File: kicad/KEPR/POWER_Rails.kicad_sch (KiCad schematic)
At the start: 21 parts, among them J1 PINHD_1x20_Male, J12 PINHD_1x20_Male, J13 PINHD_1x20_Male, J14 PINHD_1x20_Male, J15 PINHD_1x20_Male, J16 PINHD_1x10_Male, J17 PINHD_1x20_Male, J18 PINHD_1x20_Male, J19 PINHD_1x20_Male, J2 PINHD_1x20_Male, J20 PINHD_1x20_Male, J21 PINHD_1x20_Male, J22 PINHD_1x20_Male, J23 PINHD_1x10_Male, J24 PINHD_2x3_Male, J25 PINHD_2x3_Male, J26 PINHD_2x3_Male, J27 PINHD_2x3_Male, J28 PINHD_2x3_Male, J29 PINHD_2x3_Male, J30 PINHD_2x3_Male

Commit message: mais ajustes no power rail inclusive com imagem 3d
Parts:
- removed J14, J15, J21, J22: PINHD_1x20_Male, Connector_PinHeader_2.54mm:PinHeader_1x20_P2.54mm_Vertical, symbol PCM_SL_Pin_Headers:PINHD_1x20_Male
- removed J28, J29: PINHD_2x3_Male, Connector_PinHeader_2.54mm:PinHeader_2x03_P2.54mm_Vertical, symbol PCM_SL_Pin_Headers:PINHD_2x3_Male
- added J14: PINHD_2x3_Male, Connector_PinHeader_2.54mm:PinHeader_2x03_P2.54mm_Vertical, symbol PCM_SL_Pin_Headers:PINHD_2x3_Male
- added J15, J21: PINHD_1x10_Male, Connector_PinHeader_2.54mm:PinHeader_1x10_P2.54mm_Vertical, symbol PCM_SL_Pin_Headers:PINHD_1x10_Male
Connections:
- net +12V: now also J14.2
- net +3.3V: now also J14.6
- net +5V: now also J14.4
- net GND: now also J21.1, J21.10, J21.2, J21.3, J21.4, J21.5, J21.6, J21.7, J21.8, J21.9
- new net: J14.1, J14.3, J14.5, J15.1, J15.10, J15.2, J15.3, J15.4, J15.5, J15.6, J15.7, J15.8, J15.9
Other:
- moved on the sheet: J1, J12, J16, J17, J18, J19, J2, J20, J23, J24, J25, J26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

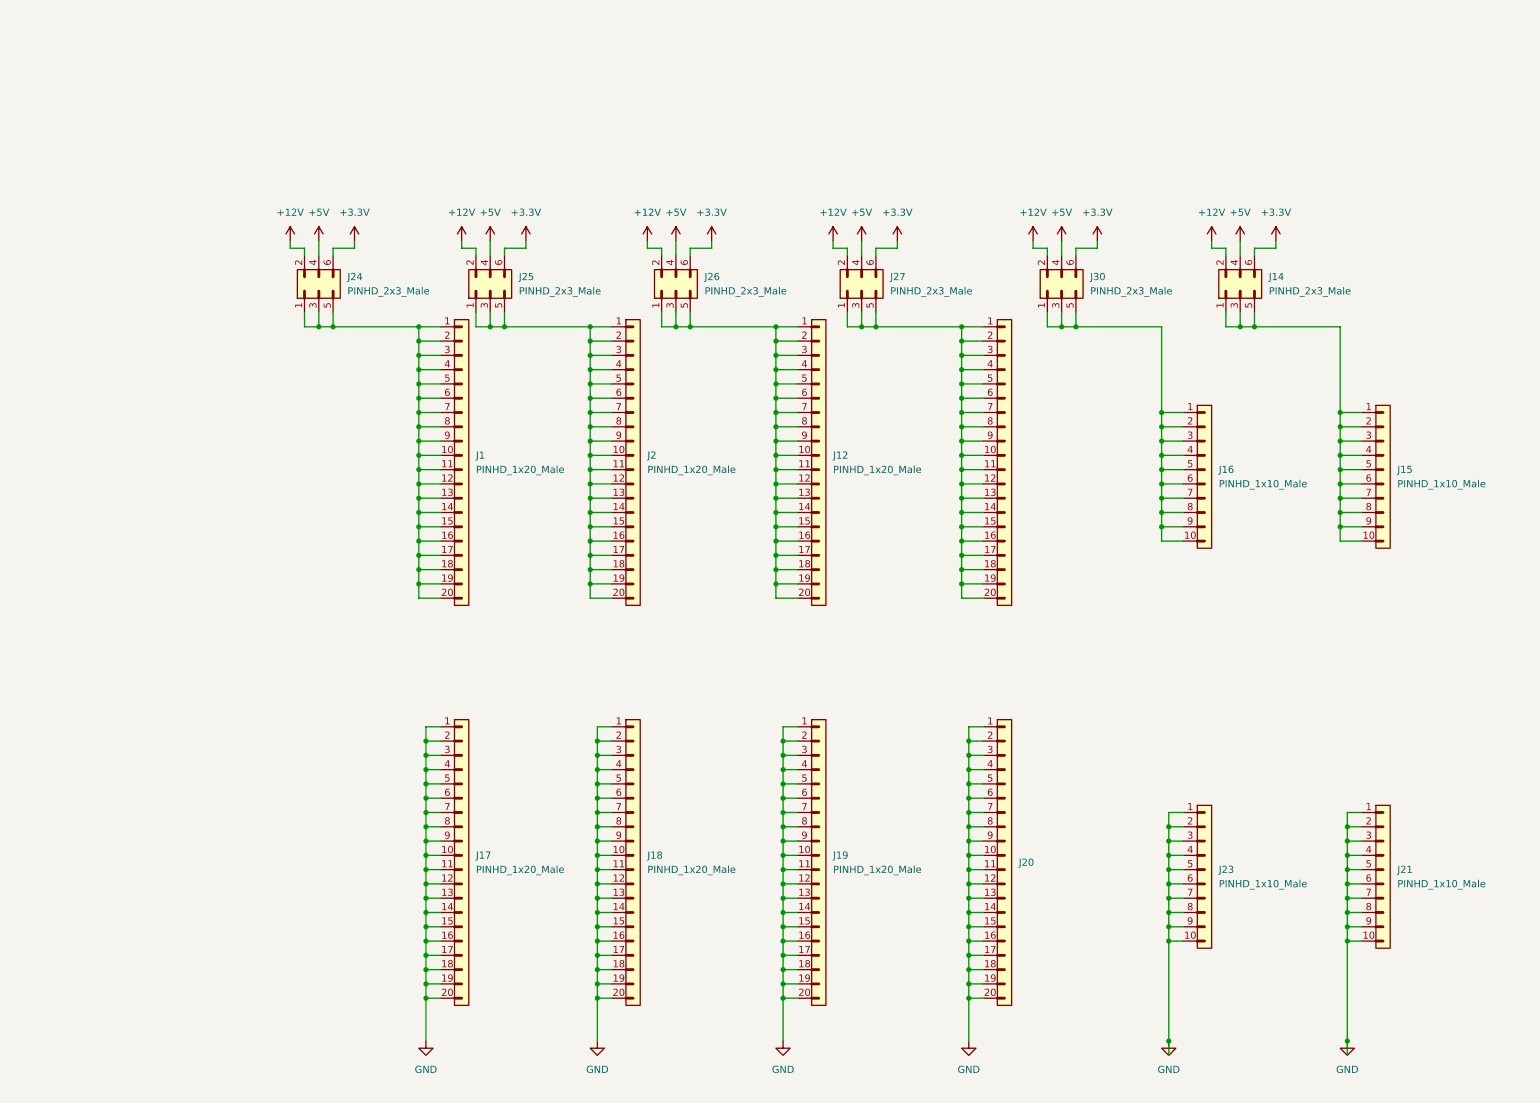
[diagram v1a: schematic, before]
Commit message: Mais ajustes nas folhas de esquemático no Power Rails
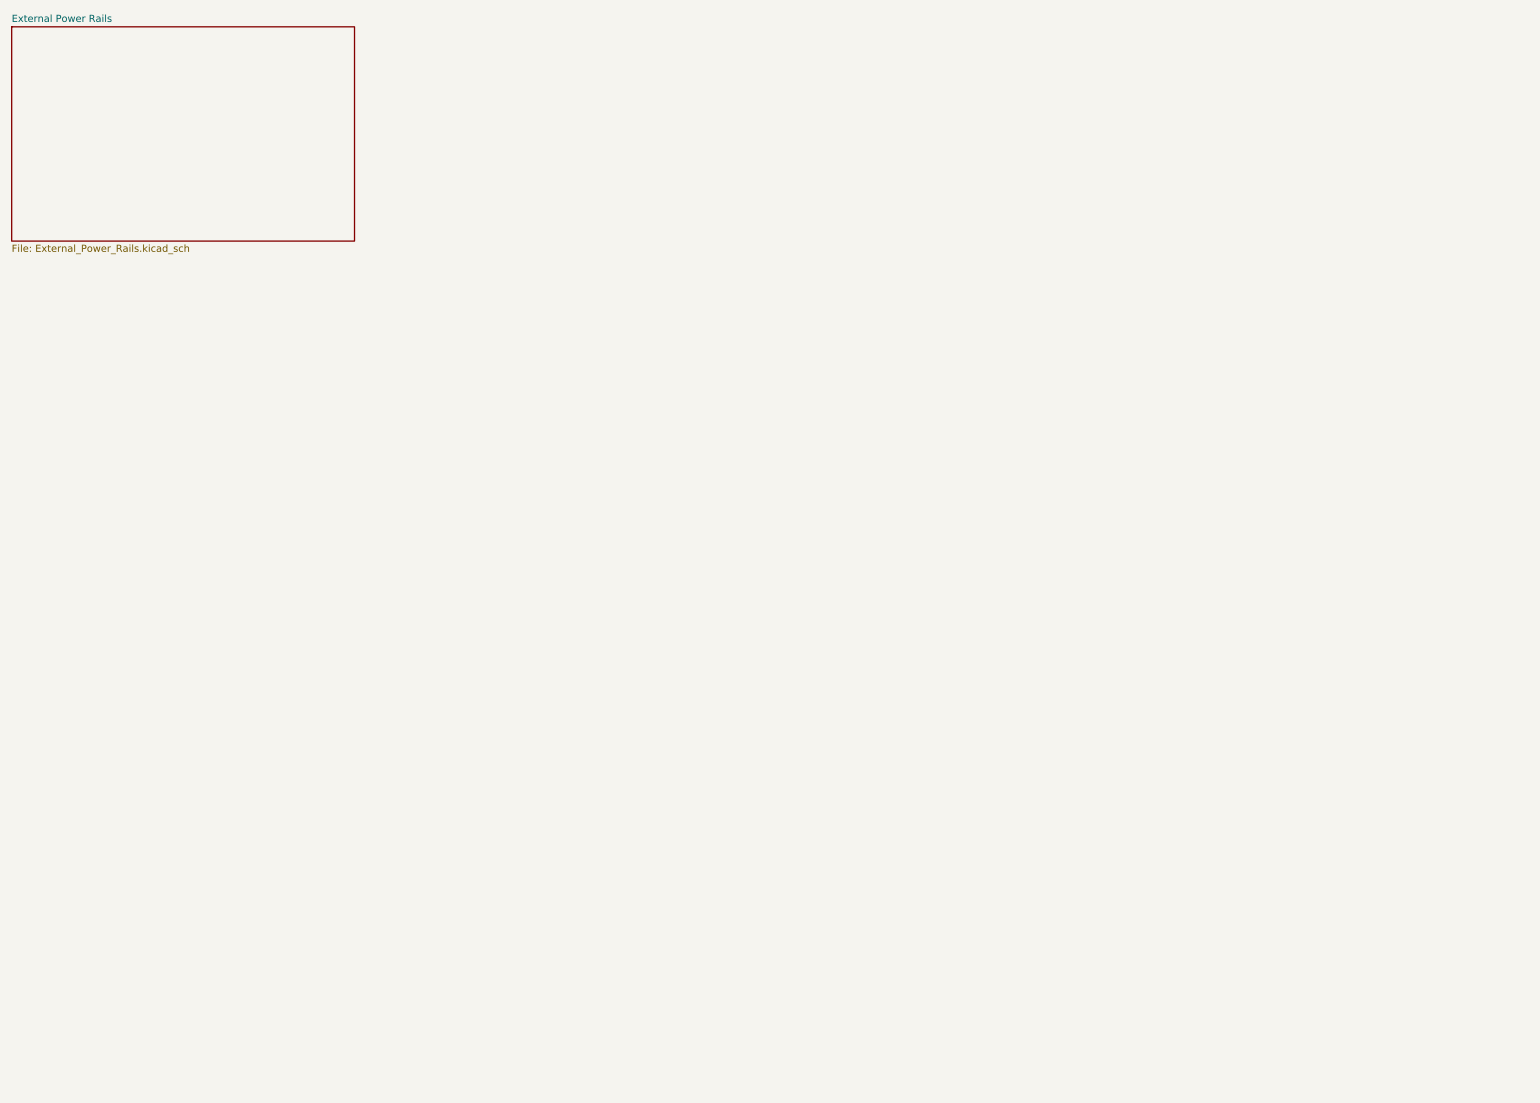
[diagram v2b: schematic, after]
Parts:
- removed J1, J12, J13, J17, J18, J19, J2, J20: PINHD_1x20_Male, Connector_PinHeader_2.54mm:PinHeader_1x20_P2.54mm_Vertical, symbol PCM_SL_Pin_Headers:PINHD_1x20_Male
- removed J14, J24, J25, J26, J27, J30: PINHD_2x3_Male, Connector_PinHeader_2.54mm:PinHeader_2x03_P2.54mm_Vertical, symbol PCM_SL_Pin_Headers:PINHD_2x3_Male
- removed J15, J16, J21, J23: PINHD_1x10_Male, Connector_PinHeader_2.54mm:PinHeader_1x10_P2.54mm_Vertical, symbol PCM_SL_Pin_Headers:PINHD_1x10_Male
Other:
- added sheet External Power Rails (External_Power_Rails.kicad_sch)

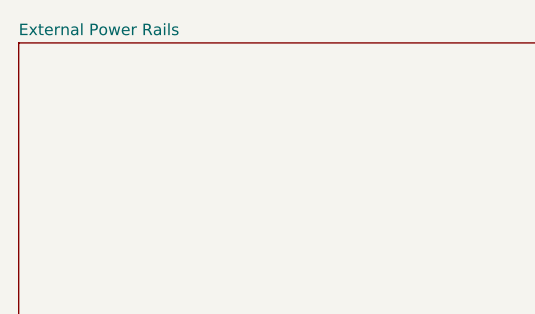
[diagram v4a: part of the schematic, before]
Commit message: Iniciado a distribuição das vias.
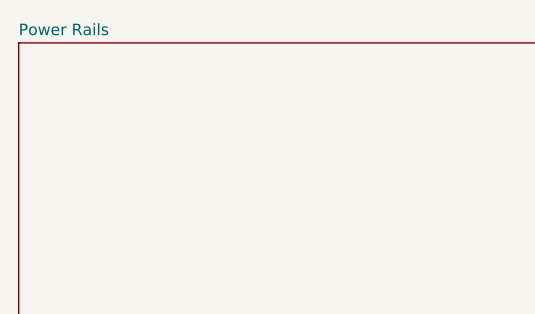
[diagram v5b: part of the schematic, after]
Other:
- sheet External Power Rails renamed Power Rails
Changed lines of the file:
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@@
 			(color 0 0 0 0.0000)
 		)
-		(property "Sheetname" "External Power Rails"
+		(property "Sheetname" "Power Rails"
 			(at 35.56 24.6884 0)
 			(show_name yes)
